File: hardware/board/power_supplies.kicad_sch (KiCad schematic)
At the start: 41 parts, among them J4 Barrel_Jack_Switch, U2 LP2985-3.3, U6 LM27762, U8 LT3506

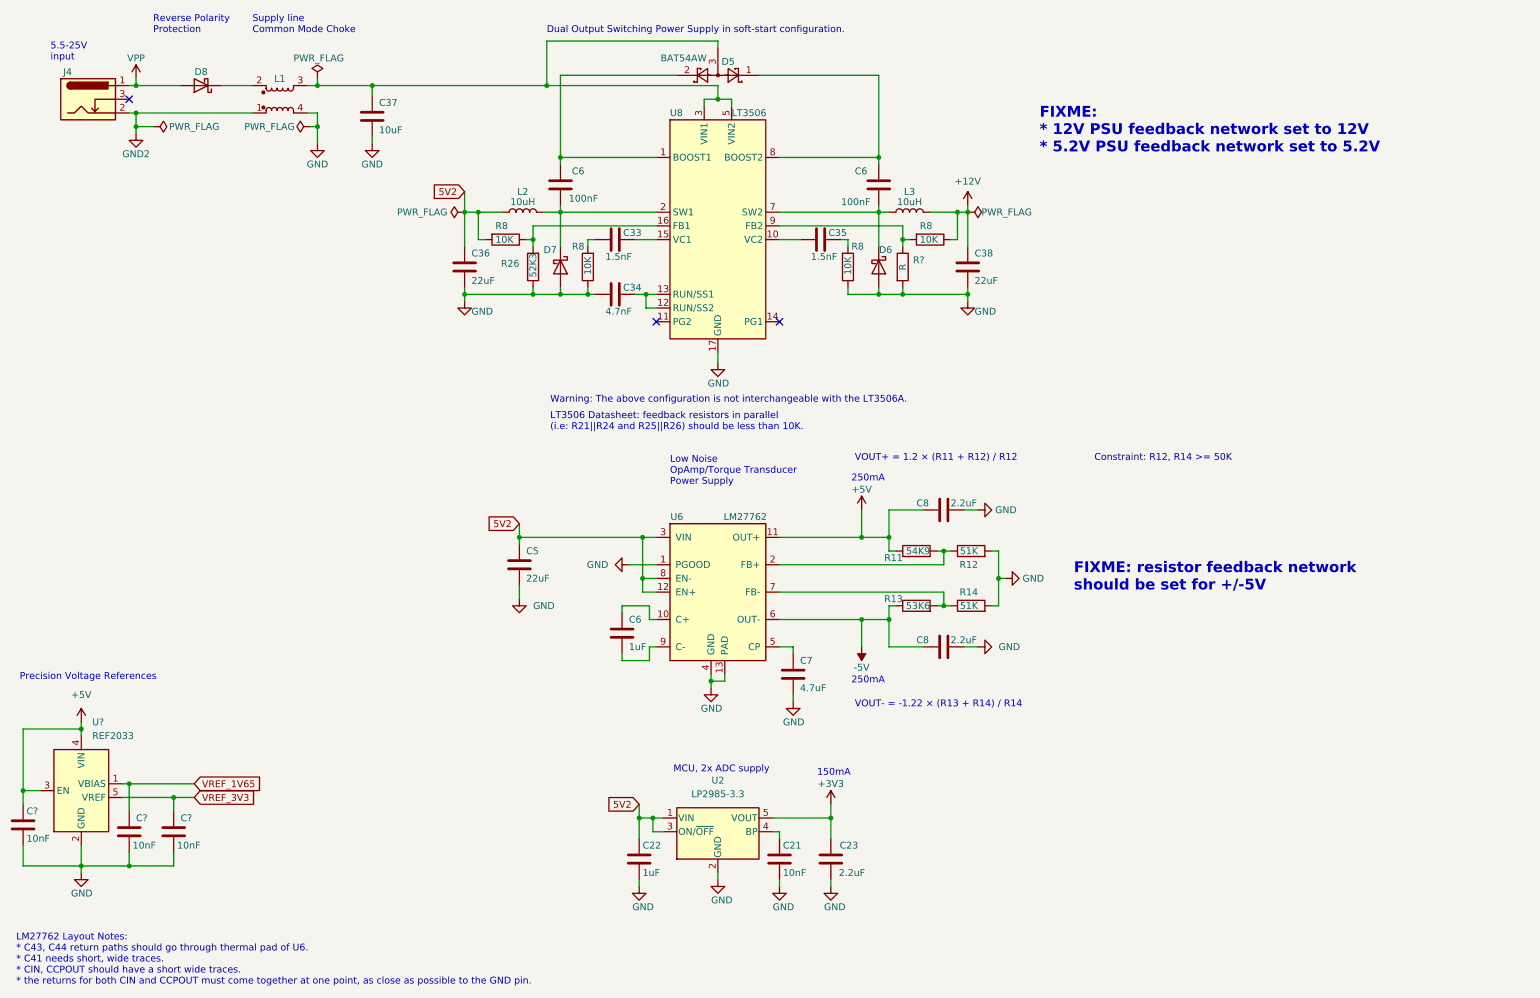
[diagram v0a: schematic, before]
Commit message: update schematic
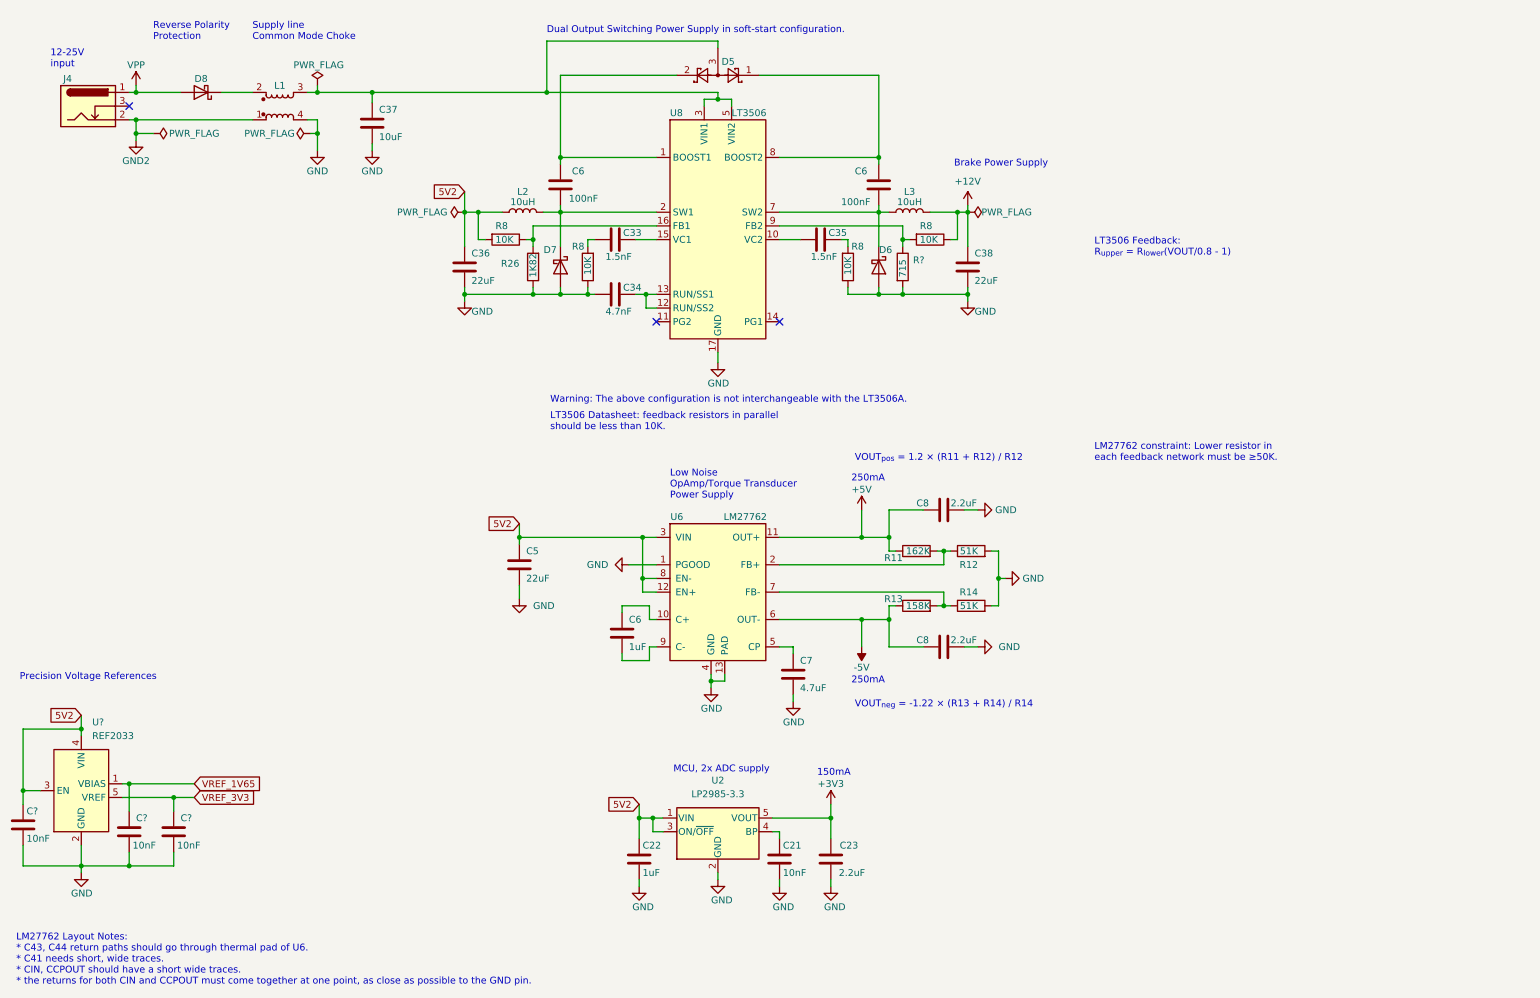
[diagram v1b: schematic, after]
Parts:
- R11: value 54K9 -> 162K; Link https://www.digikey.com/en/products/detail/panasonic-electr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 -> https://www.digikey.com/en/products/detail/yageo/RT0402BRD0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; Manufacturer Panasonic Electronic Components -> Yageo; Manufacturer Number ERA-2AEB5492X -> RT0402BRD07162KL
- R13: value 53K6 -> 158K; Link https://www.digikey.com/en/products/detail/panasonic-electr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 -> https://www.digikey.com/en/products/detail/te-connectivity-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; Manufacturer Panasonic Electronic Components -> TE Connectivity Passive Product; Manufacturer Number ERA-2AEB5362X -> RP73PF1E158KBTD; Tolerance 0.1 -> 0.1%
- R26: value 52K3 -> 1K82; Link https://www.digikey.com/en/products/detail/yageo/RT0402FRE0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 -> https://www.digikey.com/en/products/detail/yageo/RT0402BRB0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; Manufacturer Number RT0402FRE0752K3L -> RT0402BRB071K82L
- R?: value R -> 715; footprint (none) -> Resistor_SMD:R_0402_1005Metric; Link (none) -> https://www.digikey.com/en/products/detail/yageo/RC0402FR-0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; Manufacturer (none) -> Yageo; Manufacturer Number (none) -> RC0402FR-07715RL
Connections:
- net +5V: no longer C?.1, U?.3 (EN), U?.4 (VIN)
- net 5V2: now also C?.1, U?.3 (EN), U?.4 (VIN)
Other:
- note added: "12-25V input"
- note added: "Brake Power Supply"
- note added: "LM27762 constraint: Lower resistor in each feedback network must be ≥50K."
- note added: "LT3506 Datasheet: feedback resistors in parallel should be less than 10K."
- note added: "LT3506 Feedback: R_{upper} = R_{lower}(VOUT/0.8 - 1)"
- note added: "VOUT_{neg} = -1.22 × (R13 + R14) / R14"
- note added: "VOUT_{pos} = 1.2 × (R11 + R12) / R12"
- note removed: "5.5-25V input"
- note removed: "Constraint: R12, R14 >= 50K"
- note removed: "FIXME: * 12V PSU feedback network set to 12V * 5.2V PSU feedback network set to 5.2V"
- note removed: "FIXME: resistor feedback network should be set for +/-5V"
- note removed: "LT3506 Datasheet: feedback resistors in parallel (i.e: R21||R24 and R25||R26) should be less than 10K."
- note removed: "VOUT+ = 1.2 × (R11 + R12) / R12"
- note removed: "VOUT- = -1.22 × (R13 + R14) / R14"
- moved on the sheet: C37, D8, J4, L1

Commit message: update pcb
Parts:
- U?: symbol machine_agency_components:REF20xx -> kicad_component_library:REF20xx
- gave numbers to parts that had none: 1
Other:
- moved on the sheet: J4

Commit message: update sch and pcb
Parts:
- removed C5: 22uF, Capacitor_SMD:C_0805_2012Metric, symbol Device:C
- removed C? (x3): 10nF, symbol Device:C
- added C12 (x3): 100nF, Capacitor_SMD:C_0402_1005Metric, symbol Device:C
- added C38: 22uF, Capacitor_SMD:C_0805_2012Metric, symbol Device:C
- added C61: 1uF, Capacitor_SMD:C_0402_1005Metric, symbol Device:C
- C37: Alternate (none) -> GRM21BR61H106KE43L; Link https://www.digikey.com/en/products/detail/murata-electronics/GRM21BZ71E106KE15L/13904911 -> https://www.digikey.com/en/products/detail/murata-electronics/GRM21BR61H106KE43L/10326316; Manufacturer Number GRM21BZ71E106KE15L -> GRM21BR61H106KE43L; Rated Voltage 25V -> 50V; Temperature Coefficient X7R -> X5R; Tolerance (none) -> 10%
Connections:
- net 5V2: now also C12.2, C38.1, C61.1
- net GND: now also C12.1, C12.1, C12.1, C38.2, C61.2
- net VREF_1V65: now also C12.2
- net VREF_3V3: now also C12.2
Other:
- note added: "13-25V input"
- note added: "Dual Voltage Reference"
- note added: "Dual Voltage Reference Bypass Caps"
- note added: "FIXME: are these set correctly for +/-5V?"
- note added: "LT3506 Datasheet: "feedback resistors in parallel should be less than 10K.""
- note added: "VOUT_{neg} = -1.22 × (R_{top} + R_{bot}) / R_{bot}"
- note added: "VOUT_{pos} = 1.2 × (R_{top} + R_{bot}) / R_{bot}"
- note removed: "12-25V input"
- note removed: "LM27762 Layout Notes: * C43, C44 return paths should go through thermal pad of U6. * C41 needs short, wide traces. * CIN, CCPOUT should have a short wide traces. * the returns for both CIN and CCPOUT must come together at one point, as close as possible to the GND pin."
- note removed: "LT3506 Datasheet: feedback resistors in parallel should be less than 10K."
- note removed: "Precision Voltage References"
- note removed: "VOUT_{neg} = -1.22 × (R13 + R14) / R14"
- note removed: "VOUT_{pos} = 1.2 × (R11 + R12) / R12"
- moved on the sheet: C21, C22, C23, C6, C7, C8, R11, R12, R13, R14, U2, U6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

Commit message: update schematic; continue pcb draft
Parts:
- R8: Notes DNP -> (none)
- renumbered R32 to R29
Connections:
- net +12V: now also C36.1, L2.1, R8.2; no longer C38.1, L3.2, R8.1
- net 5V2: now also C38.1, L3.2, R8.1; no longer C36.1, L2.1, R8.2
- net at C6.2, U8.8 (BOOST2): now also D5.2; no longer D5.1
- net at C6.2, U8.1 (BOOST1): now also D5.1; no longer D5.2
- net at R8.1, U8.16 (FB1): now also R29.1; no longer R26.2
- net at R8.2, U8.9 (FB2): now also R26.2; no longer R29.1
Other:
- moved on the sheet: C33, C34, C35, C36, C37, C38, C6, D5, D6, D7, D8, J4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

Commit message: update schematic annotation
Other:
- note removed: "FIXME: are these set correctly for +/-5V?"
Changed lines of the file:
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@@
     (effects (font (size 1.27 1.27)) (justify left bottom))
-  )
-  (text "FIXME: are these set correctly for +/-5V?" (at 213.868 123.952 0)
-    (effects (font (size 2 2) (thickness 0.4) bold) (justify left bottom))
   )
   (text "LT3506 Feedback: \nR_{upper} = R_{lower}(VOUT/0.8 - 1)"

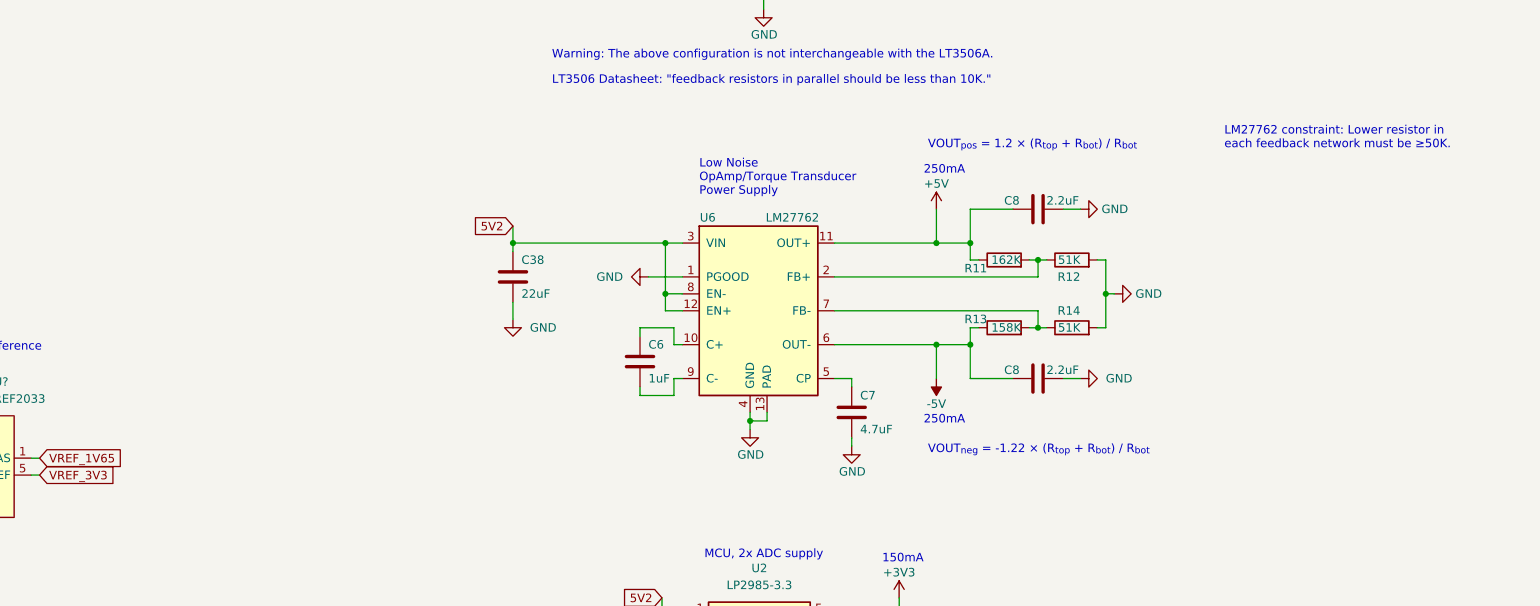
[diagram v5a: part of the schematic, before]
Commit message: draft layout with analog brake driver circuit
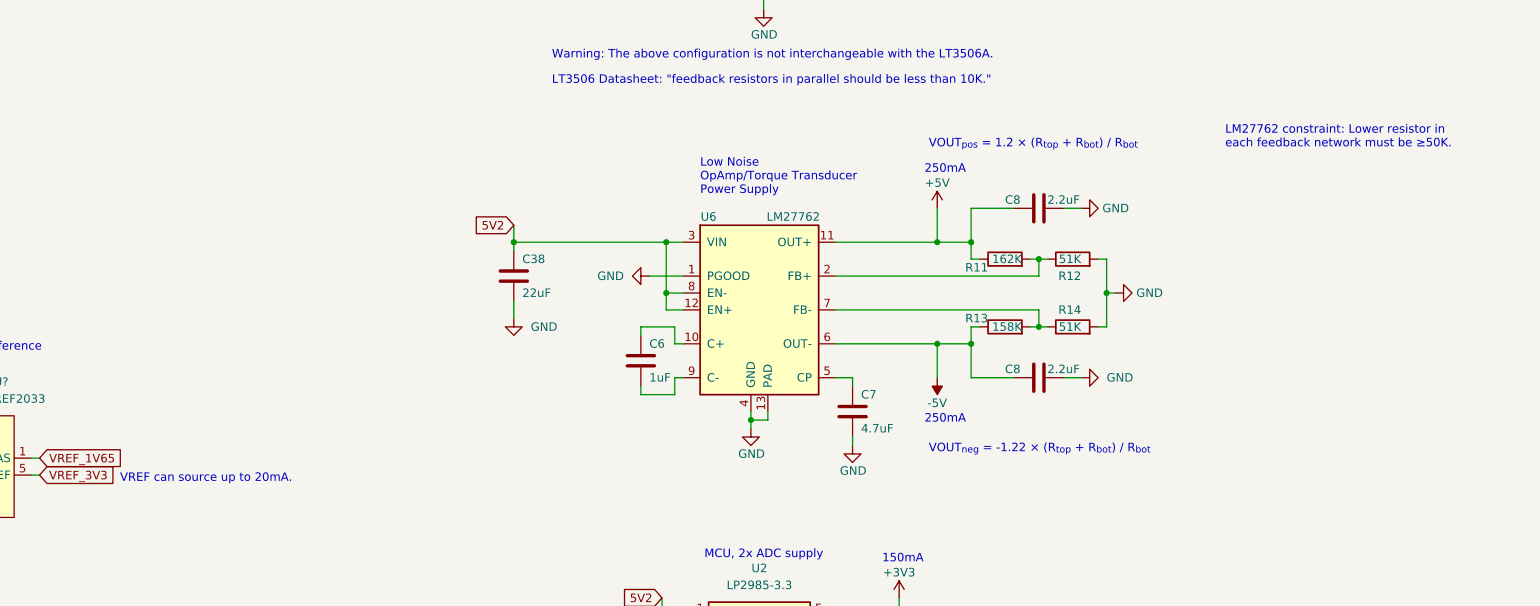
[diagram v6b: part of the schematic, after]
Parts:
- L2, L3: Manufacturer (none) -> Vishay Dale; Manufacturer Number (none) -> IHLP2525CZER100M11
- R8: Tolerance (none) -> 1%
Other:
- note added: "VREF can source up to 20mA."

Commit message: draft v0.1 pcb
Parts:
- D6, D7, D8: Manufacturer (none) -> SMC Diode Solutions
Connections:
- net at C35.1, U8.10 (VC2): now also U8.14 (PG1)
- no-connect marks 3 -> 2
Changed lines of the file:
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@@
   (junction (at 42.545 28.575) (diameter 0) (color 0 0 0 0)
   )
+  (junction (at 158.115 55.88) (diameter 0) (color 0 0 0 0)
+  )
   (junction (at 70.485 28.575) (diameter 0) (color 0 0 0 0)
   )
@@
   (no_connect (at 32.385 31.115))
   (no_connect (at 133.35 71.12))
-  (no_connect (at 156.21 71.12))
   (wire (pts (xy 168.91 55.88) (xy 168.91 57.15))
     (stroke (width 0) (type default))
@@
     (stroke (width 0) (type default))
   )
+  (wire (pts (xy 158.115 55.88) (xy 160.02 55.88))
+    (stroke (width 0) (type default))
+  )
   (wire (pts (xy 115.57 66.04) (xy 120.65 66.04))
     (stroke (width 0) (type default))
@@
     (stroke (width 0) (type default))
   )
+  (wire (pts (xy 156.21 71.12) (xy 158.115 71.12))
+    (stroke (width 0) (type default))
+  )
   (wire (pts (xy 196.215 126.365) (xy 194.945 126.365))
     (stroke (width 0) (type default))
@@
     (stroke (width 0) (type default))
   )
+  (wire (pts (xy 158.115 71.12) (xy 158.115 55.88))
+    (stroke (width 0) (type default))
+  )
   (wire (pts (xy 107.315 113.665) (xy 107.315 114.935))
     (stroke (width 0) (type default))
@@
     (stroke (width 0) (type default))
   )
-  (wire (pts (xy 156.21 55.88) (xy 160.02 55.88))
+  (wire (pts (xy 156.21 55.88) (xy 158.115 55.88))
     (stroke (width 0) (type default))
   )
@@
       (effects (font (size 1.27 1.27)) hide)
     )
-    (property "Datasheet" "~" (at 174.625 60.96 0)
+    (property "Datasheet" "https://www.smc-diodes.com/propdf/MBR260HW%20N1503%20REV.B.pdf" (at 174.625 60.96 0)
       (effects (font (size 1.27 1.27)) hide)
     )
@@
       (effects (font (size 1.27 1.27)) hide)
     )
+    (property "Manufacturer" "SMC Diode Solutions" (at 174.625 60.96 0)
+      (effects (font (size 1.27 1.27)) hide)
+    )
     (pin "1")
     (pin "2")
@@
       (effects (font (size 1.27 1.27)) hide)
     )
-    (property "Datasheet" "~" (at 115.57 60.96 0)
+    (property "Datasheet" "https://www.smc-diodes.com/propdf/MBR260HW%20N1503%20REV.B.pdf" (at 115.57 60.96 0)
       (effects (font (size 1.27 1.27)) hide)
     )
@@
       (effects (font (size 1.27 1.27)) hide)
     )
+    (property "Manufacturer" "SMC Diode Solutions" (at 115.57 60.96 0)
+      (effects (font (size 1.27 1.27)) hide)
+    )
     (pin "1")
     (pin "2")
@@
       (effects (font (size 1.27 1.27)) hide)
     )
-    (property "Datasheet" "~" (at 48.895 28.575 0)
+    (property "Datasheet" "https://www.smc-diodes.com/propdf/MBR260HW%20N1503%20REV.B.pdf" (at 48.895 28.575 0)
       (effects (font (size 1.27 1.27)) hide)
     )
@@
       (effects (font (size 1.27 1.27)) hide)
     )
+    (property "Manufacturer" "SMC Diode Solutions" (at 48.895 28.575 0)
+      (effects (font (size 1.27 1.27)) hide)
+    )

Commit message: update silkscreen size; add mating connector note
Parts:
- added C69: 10uF, Capacitor_SMD:C_0805_2012Metric, symbol Device:C
- gave numbers to parts that had none: 1
- renumbered C12 to C34, C12 to C35, C12 to C36, C6 to C44, C7 to C47, C8 to C51, C8 to C60, R11 to R33, R13 to R34, R12 to R36, R14 to R37, U6 to U13
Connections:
- net GND2: now also C69.2
- net at D8.1 (K), L1.2: now also C69.1
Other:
- moved on the sheet: C37, D8, L1
